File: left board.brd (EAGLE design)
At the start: 100 x 80 mm, 54 parts, among them IC1 LM555D, IC2 LM555D, Q3 BSS101, Q4 BSS101

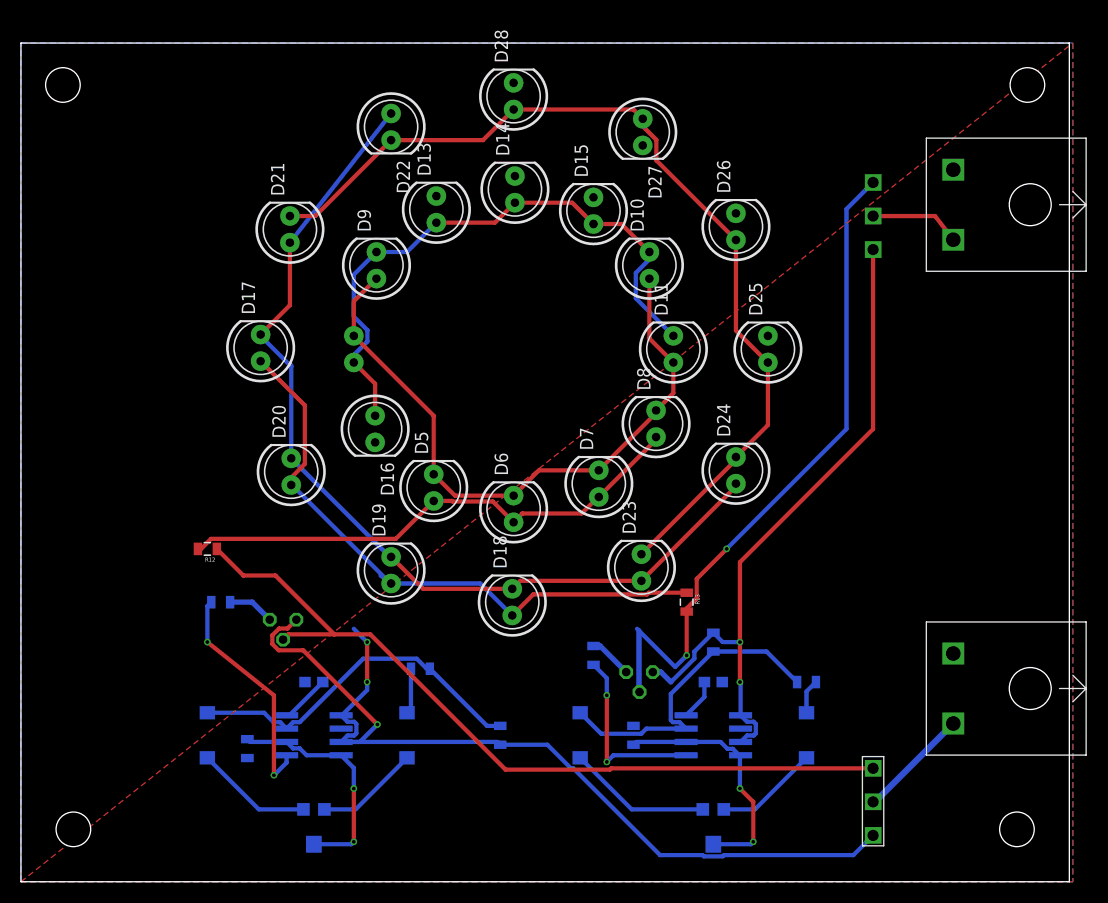
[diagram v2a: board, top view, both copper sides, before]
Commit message: added reverse polairity protection
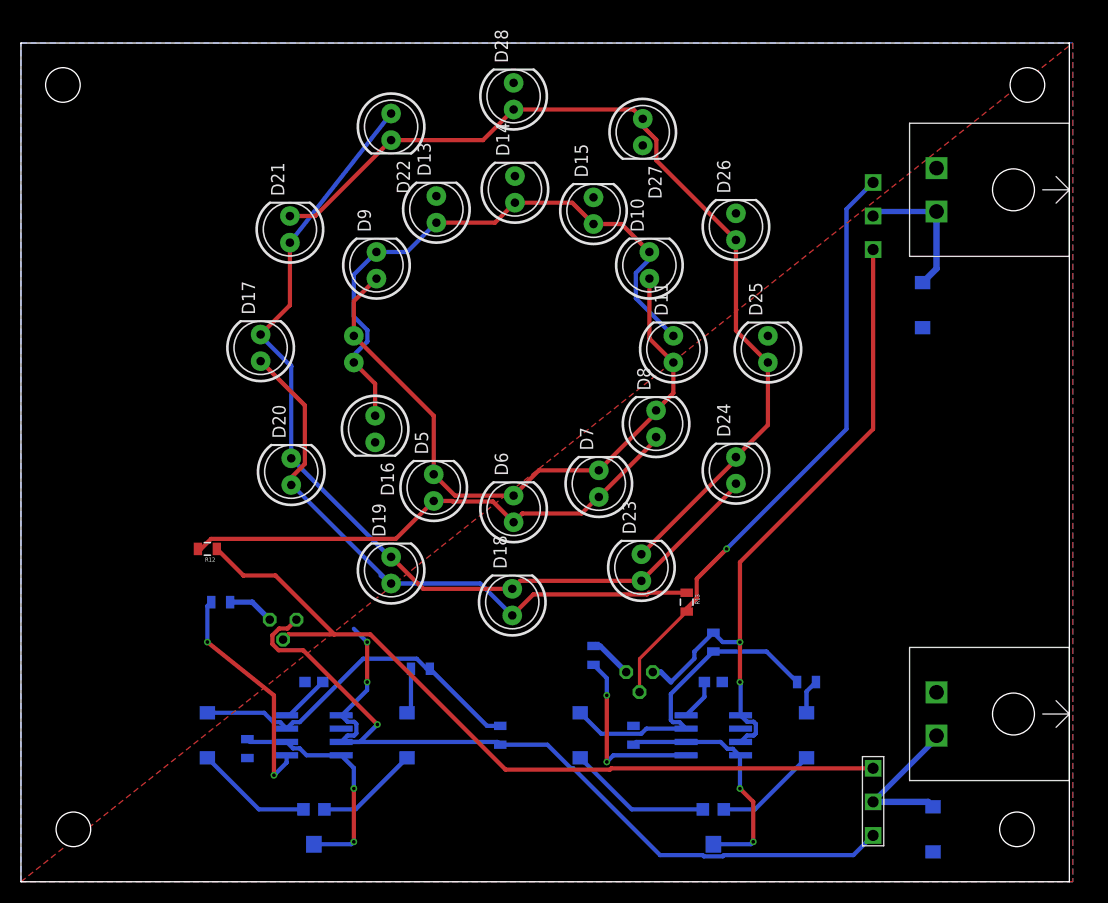
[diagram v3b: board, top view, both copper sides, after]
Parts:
- removed L_BLINK, L_DRIVE: 2_PIN_TECONNECTOR, TE 2-pin connector:2_PIN_CONNECT
- added D1, D2: MBRA140, SparkFun-DiscreteSemi:SMA-DIODE
- added U$5, U$7: 2_PIN_TECONNECTOR, TE 2-pin connector:2_PIN_CONNECT
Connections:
- net BLINK: now also D1.C, U$7.V/SIG; no longer L_BLINK.V/SIG
- net DRIVE: now also D2.C, U$5.V/SIG; no longer L_DRIVE.V/SIG
- net GND: now also D1.A, D2.A, U$5.G/LOW, U$7.G/LOW; no longer L_BLINK.G/LOW, L_DRIVE.G/LOW
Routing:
- net D_OUT: track 65.1 -> 57.8 mm, vias 2 -> 1
- net DRIVE: track 8.76 -> 13.6 mm
- net BLINK: track 10.7 -> 14.9 mm
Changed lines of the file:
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@@
 <?xml version="1.0" encoding="utf-8"?>
 <!DOCTYPE eagle SYSTEM "eagle.dtd">
-<eagle version="8.3.1">
+<eagle version="8.6.1">
 <drawing>
 <settings>
@@
 <layer number="230" name="230bmp" color="7" fill="1" visible="yes" active="yes"/>
 <layer number="231" name="231bmp" color="7" fill="1" visible="yes" active="yes"/>
+<layer number="232" name="Eagle3D_PG2" color="7" fill="1" visible="no" active="no"/>
+<layer number="233" name="Eagle3D_PG3" color="7" fill="1" visible="no" active="no"/>
 <layer number="248" name="Housing" color="7" fill="1" visible="yes" active="yes"/>
 <layer number="249" name="Edge" color="7" fill="1" visible="yes" active="yes"/>
@@
 <param name="dpMaxLengthDifference" value="10mm"/>
 <param name="dpGapFactor" value="2.5"/>
-<param name="checkGrid" value="0"/>
 <param name="checkAngle" value="0"/>
 <param name="checkFont" value="1"/>
 <param name="checkRestrict" value="0"/>
+<param name="checkStop" value="0"/>
+<param name="checkValues" value="0"/>
 <param name="useDiameter" value="13"/>
 <param name="maxErrors" value="50"/>
@@
 <element name="IC1" library="linear" library_urn="urn:adsk.eagle:library:262" package="SO08" package3d_urn="urn:adsk.eagle:package:16404/2" value="LM555D" x="27.94" y="13.97" rot="MR270"/>
 <element name="IC2" library="linear" library_urn="urn:adsk.eagle:library:262" package="SO08" package3d_urn="urn:adsk.eagle:package:16404/2" value="LM555D" x="66.04" y="13.97" rot="MR270"/>
-<element name="L_BLINK" library="TE 2-pin connector" package="2_PIN_CONNECT" value="2_PIN_TECONNECTOR" x="101.6" y="18.43" rot="R90"/>
-<element name="L_DRIVE" library="TE 2-pin connector" package="2_PIN_CONNECT" value="2_PIN_TECONNECTOR" x="101.6" y="64.58" rot="R90"/>
 <element name="U$1" library="slide switch" package="MYPART3" value="JS_SERIES_SLIDESWITCCH" x="81.28" y="7.62" rot="R90"/>
 <element name="U$2" library="slide switch" package="MYPART3" value="JS_SERIES_SLIDESWITCCH" x="81.28" y="63.5" rot="MR90"/>
@@
 <element name="Q3" library="transistor-fet" library_urn="urn:adsk.eagle:library:396" package="TO92" package3d_urn="urn:adsk.eagle:package:28523/1" value="BSS101" x="25" y="25" rot="MR180"/>
 <element name="Q4" library="transistor-fet" library_urn="urn:adsk.eagle:library:396" package="TO92" package3d_urn="urn:adsk.eagle:package:28523/1" value="BSS101" x="59" y="20" rot="MR180"/>
+<element name="U$5" library="TE 2-pin connector" package="2_PIN_CONNECT" value="2_PIN_TECONNECTOR" x="100" y="66" rot="R90"/>
+<element name="U$7" library="TE 2-pin connector" package="2_PIN_CONNECT" value="2_PIN_TECONNECTOR" x="100" y="16" rot="R90"/>
+<element name="D1" library="SparkFun-DiscreteSemi" package="SMA-DIODE" value="MBRA140" x="87" y="5" rot="MR90">
+<attribute name="PROD_ID" value="DIO-08053" x="87" y="5" size="1.778" layer="28" rot="MR90" display="off"/>
+</element>
+<element name="D2" library="SparkFun-DiscreteSemi" package="SMA-DIODE" value="MBRA140" x="86" y="55" rot="MR90">
+<attribute name="PROD_ID" value="DIO-08053" x="86" y="55" size="1.778" layer="28" rot="MR90" display="off"/>
+</element>
 </elements>
 <signals>
@@
 <contactref element="IC1" pad="2"/>
 <contactref element="IC2" pad="2"/>
-<contactref element="L_BLINK" pad="G/LOW"/>
-<contactref element="L_DRIVE" pad="G/LOW"/>
 <contactref element="D16" pad="K"/>
 <contactref element="D15" pad="K"/>
@@
 <vertex x="0" y="0"/>
 </polygon>
+<contactref element="U$5" pad="G/LOW"/>
+<contactref element="U$7" pad="G/LOW"/>
+<contactref element="D1" pad="A"/>
+<contactref element="D2" pad="A"/>
 </signal>
 <signal name="N$6">
@@
 </signal>
 <signal name="BLINK">
-<contactref element="L_BLINK" pad="V/SIG"/>
 <contactref element="U$1" pad="IN"/>
 <wire x1="81.28" y1="7.62" x2="81.46" y2="7.62" width="0.6096" layer="16"/>
-<wire x1="81.46" y1="7.62" x2="88.93" y2="15.09" width="0.6096" layer="16"/>
+<contactref element="U$7" pad="V/SIG"/>
+<wire x1="81.28" y1="7.62" x2="87.33" y2="13.67" width="0.508" layer="16"/>
+<wire x1="87.33" y1="13.67" x2="87.33" y2="13.93" width="0.508" layer="16"/>
+<contactref element="D1" pad="C"/>
+<wire x1="81.28" y1="7.62" x2="86.53" y2="7.62" width="0.6096" layer="16"/>
+<wire x1="86.53" y1="7.62" x2="87" y2="7.15" width="0.6096" layer="16"/>
 </signal>
 <signal name="DRIVE">
-<contactref element="L_DRIVE" pad="V/SIG"/>
 <contactref element="U$2" pad="IN"/>
-<wire x1="81.28" y1="63.5" x2="87.19" y2="63.5" width="0.4064" layer="1"/>
-<wire x1="87.19" y1="63.5" x2="88.93" y2="61.24" width="0.4064" layer="1"/>
+<contactref element="U$5" pad="V/SIG"/>
+<wire x1="81.28" y1="63.5" x2="81.71" y2="63.93" width="0.508" layer="16"/>
+<wire x1="81.71" y1="63.93" x2="87.33" y2="63.93" width="0.508" layer="16"/>
+<contactref element="D2" pad="C"/>
+<wire x1="87.33" y1="63.93" x2="87.33" y2="58.48" width="0.6096" layer="16"/>
+<wire x1="87.33" y1="58.48" x2="86" y2="57.15" width="0.6096" layer="16"/>
 </signal>
 <signal name="B_OUT">
@@
 <contactref element="U$2" pad="OUT2"/>
 <contactref element="R13" pad="2"/>
-<wire x1="62.4" y1="20.49" x2="63.5" y2="21.59" width="0.4064" layer="16"/>
-<via x="63.5" y="21.59" extent="1-16" drill="0.35"/>
-<wire x1="63.5" y1="21.59" x2="63.5" y2="25.77" width="0.4064" layer="1"/>
 <wire x1="63.5" y1="25.77" x2="63.5" y2="26.06710625" width="0.4064" layer="1"/>
 <wire x1="64.4556" y1="28.8956" x2="67.31" y2="31.75" width="0.4064" layer="1"/>
@@
 <wire x1="78.74" y1="64.1604" x2="81.28" y2="66.7004" width="0.4064" layer="16"/>
 <wire x1="78.74" y1="43.18" x2="78.74" y2="64.1604" width="0.4064" layer="16"/>
-<wire x1="58.76" y1="24.13" x2="58.945" y2="23.945" width="0.4064" layer="16"/>
 <contactref element="Q4" pad="2"/>
-<wire x1="58.945" y1="23.945" x2="62.4" y2="20.49" width="0.4064" layer="16"/>
-<wire x1="58.945" y1="23.945" x2="58.945" y2="18.15" width="0.508" layer="16"/>
-<wire x1="58.945" y1="18.15" x2="59" y2="18.095" width="0.508" layer="16"/>
+<wire x1="63.5" y1="25.77" x2="59" y2="21.27" width="0.3048" layer="1"/>
+<wire x1="59" y1="21.27" x2="59" y2="18.095" width="0.3048" layer="1"/>
 </signal>
 <signal name="D_BLINK">
